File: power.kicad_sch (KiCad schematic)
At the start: 51 parts, among them U10 TPS82084SIL, U11 TPS7A8801RTJR, U12 TPS7A8801RTJR, U9 TPS82084SIL

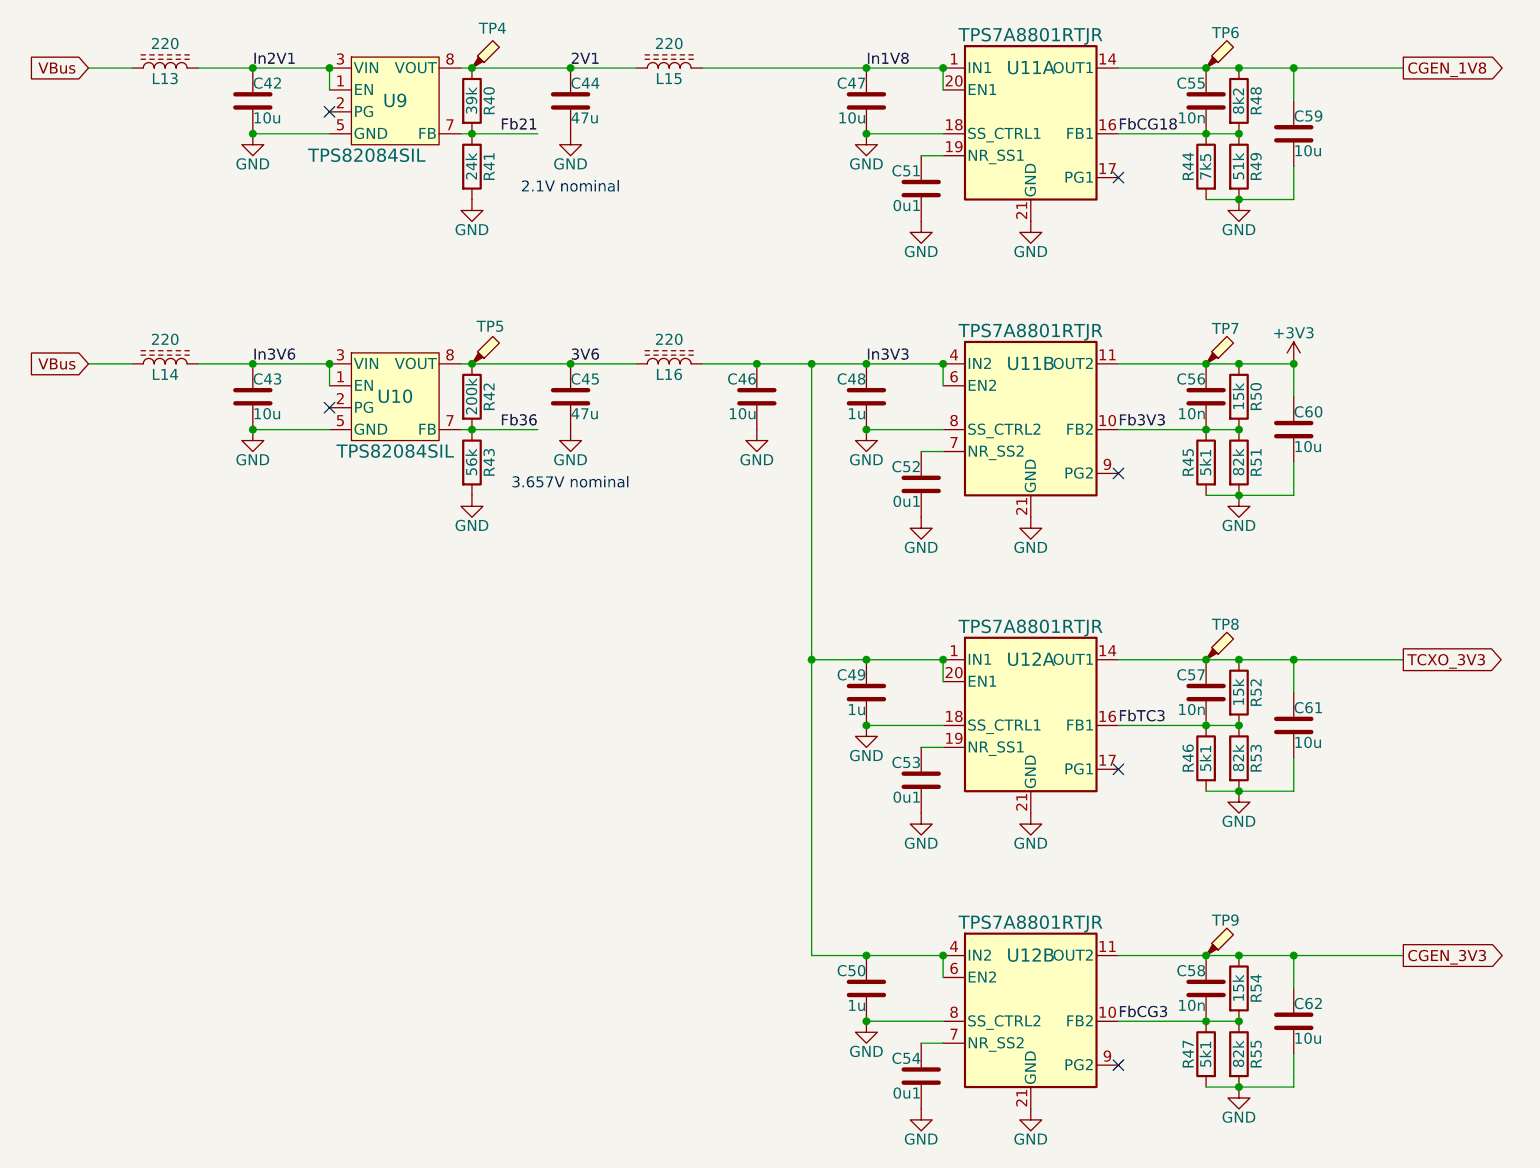
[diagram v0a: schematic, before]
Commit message: Silkscreen passes DRC.  Also we renumbered everything.
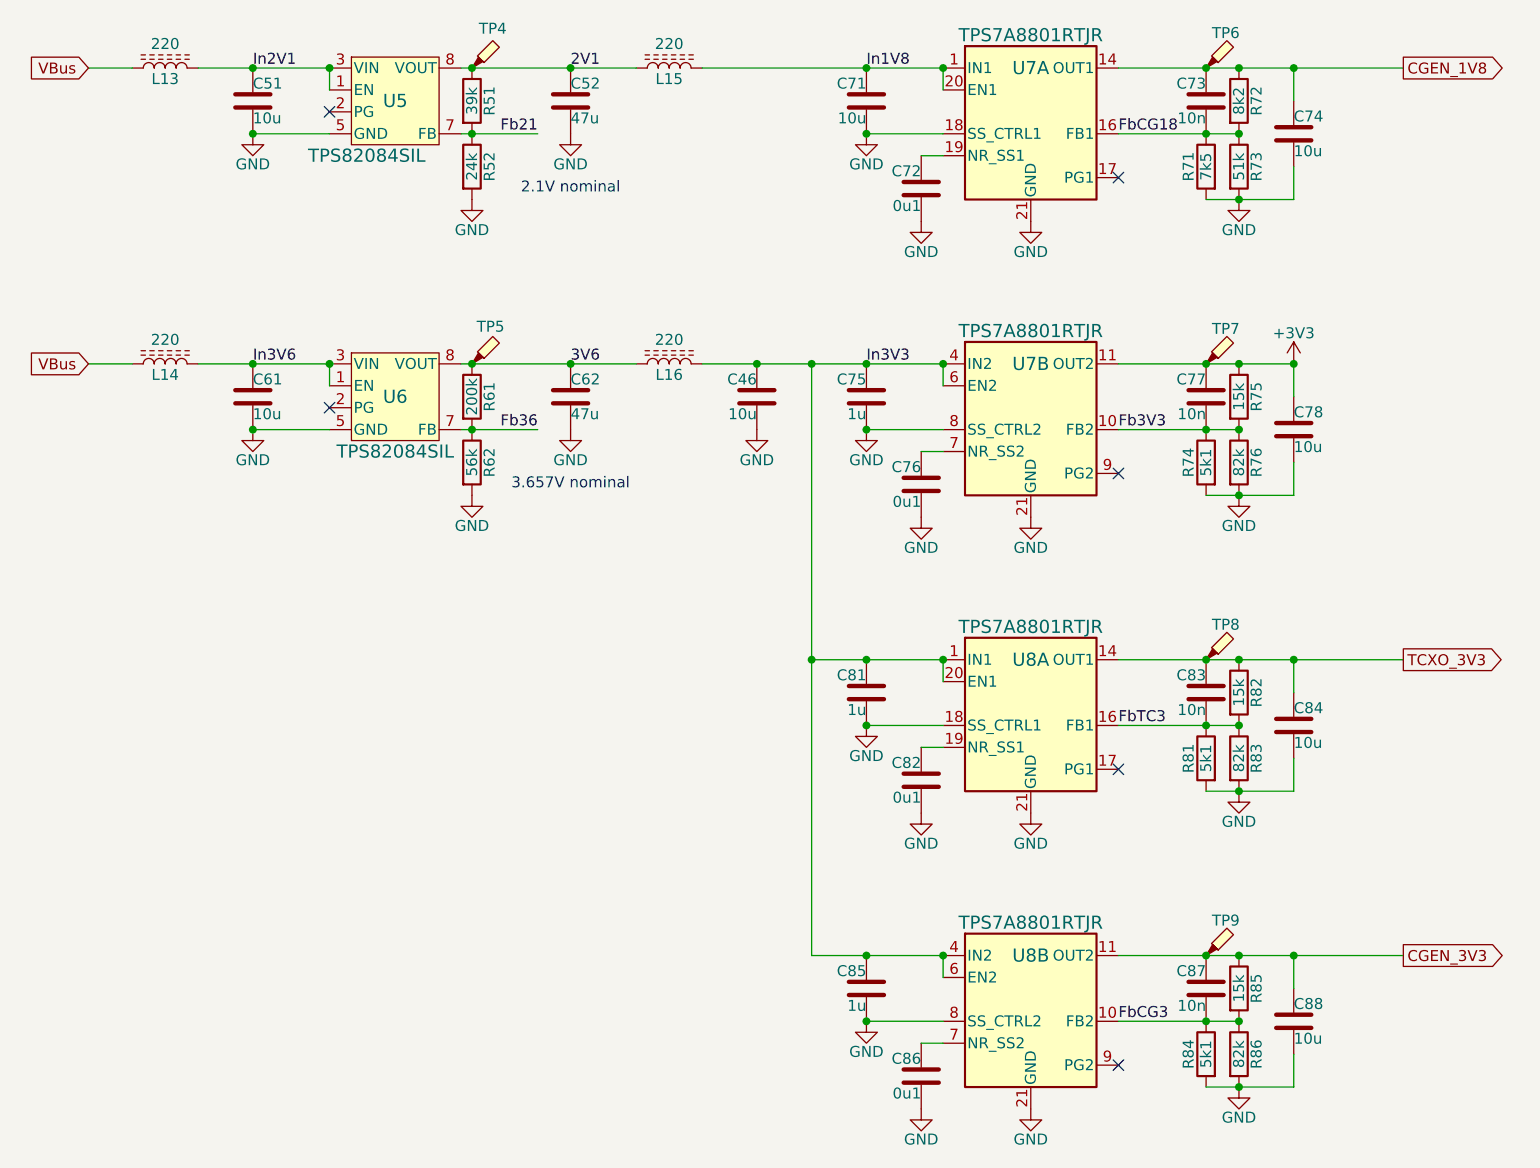
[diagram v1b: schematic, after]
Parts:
- renumbered C42 to C51, C44 to C52, C43 to C61, C45 to C62, C47 to C71, C51 to C72, C55 to C73, C59 to C74, C48 to C75, C52 to C76, C56 to C77, C60 to C78, C49 to C81, C53 to C82, C57 to C83, C61 to C84, C50 to C85, C54 to C86, C58 to C87, C62 to C88, R40 to R51, R41 to R52, R42 to R61, R43 to R62, R44 to R71, R48 to R72, R49 to R73, R45 to R74, R50 to R75, R51 to R76, R46 to R81, R52 to R82, R53 to R83, R47 to R84, R54 to R85, R55 to R86, U9 to U5, U10 to U6, U11 to U7, U12 to U8

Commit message: Sorting out part number assignments.
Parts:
- C46, C51, C61, C71, C74, C78, C84, C88: JLCPCB C15525 -> (none); LCSC (none) -> C15525
- C52, C62: JLCPCB C16780 -> (none); LCSC (none) -> C16780
- C72, C76, C82, C86: JLCPCB C307331 -> (none); LCSC (none) -> C307331
- C73, C77, C83, C87: JLCPCB C15195 -> (none); LCSC (none) -> C15195
- C75, C81, C85: JLCPCB C52923 -> (none); LCSC (none) -> C52923
- L13, L14, L15, L16: JLCPCB C14709 -> (none); LCSC (none) -> C14709
- R51: JLCPCB C25796 -> (none); LCSC (none) -> C25796
- R52: LCSC (none) -> C25769
- R61: LCSC (none) -> C25764
- R62: LCSC (none) -> C25796
- R71: JLCPCB C25918 -> (none); LCSC (none) -> C25918
- R72: JLCPCB C25924 -> (none); LCSC (none) -> C25924
- R73: JLCPCB C23196 -> (none); LCSC (none) -> C23196
- R74, R81, R84: JLCPCB C25905 -> (none); LCSC (none) -> C25905
- R75, R82, R85: JLCPCB C25756 -> (none); LCSC (none) -> C25756
- R76, R83, R86: JLCPCB C23254 -> (none); LCSC (none) -> C23254
- U5, U6: JLCPCB C468248 -> (none); LCSC (none) -> C468248
- U7, U8: JLCPCB C485919 -> (none); LCSC (none) -> C485919
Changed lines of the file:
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@@
 			)
 		)
-		(property "JLCPCB" "C25756"
-			(at 196.85 69.85 0)
+		(property "LCSC" "C25756"
+			(at 196.85 69.85 90)
 			(effects
 				(font
@@
 			)
 		)
-		(property "JLCPCB" "C307331"
+		(property "LCSC" "C307331"
 			(at 160.02 148.59 0)
 			(effects
@@
 			)
 		)
-		(property "JLCPCB" "C15525"
+		(property "LCSC" "C15525"
 			(at 203.2 39.37 0)
 			(effects
@@
 			)
 		)
-		(property "JLCPCB" "C23254"
+		(property "LCSC" "C23254"
 			(at 196.85 111.76 90)
 			(effects
@@
 			)
 		)
-		(property "JLCPCB" "C15195"
+		(property "LCSC" "C15195"
 			(at 193.04 69.85 0)
 			(effects
@@
 			)
 		)
-		(property "JLCPCB" "C23254"
+		(property "LCSC" "C23254"
 			(at 196.85 146.05 90)
 			(effects
@@
 			)
 		)
-		(property "JLCPCB" "C468248"
+		(property "LCSC" "C468248"
 			(at 99.06 35.56 0)
 			(effects
@@
 			)
 		)
-		(property "JLCPCB" "C14709"
+		(property "LCSC" "C14709"
 			(at 72.39 31.75 90)
 			(effects
@@
 			)
 		)
-		(property "JLCPCB" "C25905"
-			(at 193.04 146.05 0)
+		(property "LCSC" "C25905"
+			(at 193.04 146.05 90)
 			(effects
 				(font
@@
 			)
 		)
-		(property "JLCPCB" "C15525"
+		(property "LCSC" "C15525"
 			(at 203.2 107.95 0)
 			(effects
@@
 			)
 		)
-		(property "JLCPCB" "C14709"
+		(property "LCSC" "C14709"
 			(at 130.81 31.75 90)
 			(effects
@@
 			)
 		)
-		(property "JLCPCB" "C23196"
-			(at 196.85 43.18 0)
+		(property "LCSC" "C23196"
+			(at 196.85 43.18 90)
 			(effects
 				(font
@@
 			)
 		)
-		(property "JLCPCB" "C485919"
+		(property "LCSC" "C485919"
 			(at 172.72 38.1 0)
 			(effects
@@
 			)
 		)
-		(property "JLCPCB" "C23254"
+		(property "LCSC" "C23254"
 			(at 196.85 77.47 90)
 			(effects
@@
 			)
 		)
-		(property "JLCPCB" "C25905"
-			(at 193.04 77.47 0)
+		(property "LCSC" "C25905"
+			(at 193.04 77.47 90)
 			(effects
 				(font
@@
 			)
 		)
-		(property "JLCPCB" "C15525"
+		(property "LCSC" "C15525"
 			(at 203.2 142.24 0)
 			(effects
@@
 			)
 		)
-		(property "JLCPCB" "C25796"
-			(at 107.95 35.56 0)
+		(property "LCSC" "C25796"
+			(at 107.95 35.56 90)
 			(effects
 				(font
@@
 			)
 		)
-		(property "JLCPCB" "C15195"
+		(property "LCSC" "C15195"
 			(at 193.04 138.43 0)
 			(effects
@@
 			)
 		)
-		(property "JLCPCB" ""
-			(at 107.95 69.85 0)
+		(property "LCSC" "C25764"
+			(at 107.95 69.85 90)
 			(effects
 				(font
@@
 			)
 		)
-		(property "JLCPCB" "C52923"
+		(property "LCSC" "C52923"
 			(at 153.67 69.85 0)
 			(effects
@@
 			)
 		)
-		(property "JLCPCB" "C52923"
+		(property "LCSC" "C52923"
 			(at 153.67 104.14 0)
 			(effects
@@
 			)
 		)
-		(property "JLCPCB" "C485919"
+		(property "LCSC" "C485919"
 			(at 172.72 106.68 0)
 			(effects
@@
 			)
 		)
-		(property "JLCPCB" "C15525"
+		(property "LCSC" "C15525"
 			(at 153.67 35.56 0)
 			(effects
@@
 			)
 		)
-		(property "JLCPCB" "C25905"
-			(at 193.04 111.76 0)
+		(property "LCSC" "C25905"
+			(at 193.04 111.76 90)
 			(effects
 				(font
@@
 			)
 		)
-		(property "JLCPCB" "C16780"
+		(property "LCSC" "C16780"
 			(at 119.38 69.85 0)
 			(effects
@@
 			)
 		)
-		(property "JLCPCB" "C14709"
+		(property "LCSC" "C14709"
 			(at 72.39 66.04 90)
 			(effects
@@
 			)
 		)
-		(property "JLCPCB" "C15525"
+		(property "LCSC" "C15525"
 			(at 140.97 69.85 0)
 			(effects
@@
 			)
 		)
-		(property "JLCPCB" "C25756"
+		(property "LCSC" "C25756"
 			(at 196.85 138.43 90)
 			(effects
@@
 			)
 		)
-		(property "JLCPCB" "C485919"
+		(property "LCSC" "C485919"
 			(at 172.72 140.97 0)
 			(effects
@@
 			)
 		)
-		(property "JLCPCB" ""
-			(at 107.95 43.18 0)
+		(property "LCSC" "C25769"
+			(at 107.95 43.18 90)
 			(effects
 				(font
@@
 			)
 		)
-		(property "JLCPCB" "C25756"
+		(property "LCSC" "C25756"
 			(at 196.85 104.14 90)
 			(effects
@@
 			)
 		)
-		(property "JLCPCB" "C485919"
+		(property "LCSC" "C485919"
 			(at 172.72 72.39 0)
 			(effects
@@
 			)
 		)
-		(property "JLCPCB" "C25924"
+		(property "LCSC" "C25924"
 			(at 196.85 35.56 90)
 			(effects
@@
 			)
 		)
-		(property "JLCPCB" "C307331"
+		(property "LCSC" "C307331"
 			(at 160.02 80.01 0)
 			(effects
@@
 			)
 		)
-		(property "JLCPCB" "C16780"
+		(property "LCSC" "C16780"
 			(at 119.38 35.56 0)
 			(effects
@@
 			)
 		)
-		(property "JLCPCB" "C25918"
-			(at 193.04 43.18 0)
+		(property "LCSC" "C25918"
+			(at 193.04 43.18 90)
 			(effects
 				(font
@@
 			)
 		)
-		(property "JLCPCB" "C15195"
+		(property "LCSC" "C15195"
 			(at 193.04 104.14 0)
 			(effects
@@
 			)
 		)
-		(property "JLCPCB" "C15525"
+		(property "LCSC" "C15525"
 			(at 203.2 73.66 0)
 			(effects
@@
 			)
 		)
-		(property "JLCPCB" "C15525"
+		(property "LCSC" "C15525"
 			(at 82.55 69.85 0)
 			(effects
@@
 			)
 		)
-		(property "JLCPCB" "C15525"
+		(property "LCSC" "C15525"
 			(at 82.55 35.56 0)
 			(effects
@@
 			)
 		)
-		(property "JLCPCB" ""
-			(at 107.95 77.47 0)
+		(property "LCSC" "C25796"
+			(at 107.95 77.47 90)
 			(effects
 				(font
@@
 			)
 		)
-		(property "JLCPCB" "C15195"
+		(property "LCSC" "C15195"
 			(at 193.04 35.56 0)
 			(effects
@@
 			)
 		)
-		(property "JLCPCB" "C468248"
+		(property "LCSC" "C468248"
 			(at 99.06 69.85 0)
 			(effects
@@
 			)
 		)
-		(property "JLCPCB" "C307331"
+		(property "LCSC" "C307331"
 			(at 160.02 45.72 0)
 			(effects
@@
 			)
 		)
-		(property "JLCPCB" "C307331"
+		(property "LCSC" "C307331"
 			(at 160.02 114.3 0)
 			(effects
@@
 			)
 		)
-		(property "JLCPCB" "C14709"
+		(property "LCSC" "C14709"
 			(at 130.81 66.04 90)
 			(effects
@@
 			)
 		)
-		(property "JLCPCB" "C52923"
+		(property "LCSC" "C52923"
 			(at 153.67 138.43 0)
 			(effects

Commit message: Final fixes.  Ordered.
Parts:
- R51: LCSC C25796 -> C25783
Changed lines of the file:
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@@
 			)
 		)
-		(property "LCSC" "C25796"
+		(property "LCSC" "C25783"
 			(at 107.95 35.56 90)
+			(effects
+				(font
+					(size 1.27 1.27)
+				)
+				(hide yes)
+			)
+		)
+		(property "JLCPCB" ""
+			(at 107.95 35.56 0)
 			(effects
 				(font
@@
 			(at 119.38 35.56 0)
 			(effects
+				(font
+					(size 1.27 1.27)
+				)
+				(hide yes)
+			)
+		)
+		(property "JLCPCB" ""
+			(at 119.38 35.56 0)
+			(effects

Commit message: Schematic updates for revision mostly done.
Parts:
- C901: renamed from C81; now not fitted
- C902: renamed from C83; now not fitted
- C903: renamed from C84; now not fitted
- C904: renamed from C82; now not fitted
- C905: renamed from C85; now not fitted
- C906: renamed from C87; now not fitted
- C907: renamed from C88; now not fitted
- C908: renamed from C86; now not fitted
- R901: renamed from R82; now not fitted
- R902: renamed from R81; now not fitted
- R903: renamed from R83; now not fitted
- R904: renamed from R85; now not fitted
- R905: renamed from R84; now not fitted
- R906: renamed from R86; now not fitted
- TP901: renamed from TP8; now not fitted
- TP902: renamed from TP9; now not fitted
- U901: renamed from U8; now not fitted
- renumbered C71 to C53, C72 to C54, C73 to C55, C74 to C56, C75 to C63, C76 to C64, C77 to C65, C78 to C66, L13 to L51, L15 to L52, L14 to L53, L16 to L54, R72 to R53, R71 to R54, R73 to R55, R75 to R63, R74 to R64, R76 to R65

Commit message: Use impedance matching baluns.
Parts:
- removed C63: 1u, Capacitor_SMD:C_0402_1005Metric, symbol Device:C
- renumbered C46 to C63
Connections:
- net CGEN_1V8 renamed +1V8
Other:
- moved on the sheet: C63
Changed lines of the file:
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@@
 	)
 	(junction
+		(at 153.67 73.66)
+		(diameter 0)
+		(color 0 0 0 0)
+	)
+	(junction
 		(at 203.2 134.62)
 		(diameter 0)
@@
 	)
 	(junction
-		(at 153.67 73.66)
-		(diameter 0)
-		(color 0 0 0 0)
-	)
-	(junction
 		(at 82.55 73.66)
 		(diameter 0)
@@
 	)
 	(junction
-		(at 153.67 142.24)
-		(diameter 0)
-		(color 0 0 0 0)
-	)
-	(junction
-		(at 196.85 66.04)
+		(at 153.67 66.04)
 		(diameter 0)
 		(color 0 0 0 0)
 	)
 	(junction
-		(at 91.44 31.75)
+		(at 153.67 142.24)
 		(diameter 0)
 		(color 0 0 0 0)
 	)
 	(junction
-		(at 107.95 73.66)
+		(at 196.85 66.04)
 		(diameter 0)
 		(color 0 0 0 0)
 	)
 	(junction
-		(at 140.97 66.04)
+		(at 91.44 31.75)
 		(diameter 0)
 		(color 0 0 0 0)
 	)
 	(junction
-		(at 153.67 66.04)
+		(at 107.95 73.66)
 		(diameter 0)
 		(color 0 0 0 0)
@@
 	(wire
 		(pts
-			(xy 140.97 66.04) (xy 147.32 66.04)
-		)
-		(stroke
-			(width 0)
-			(type default)
-		)
-	)
-	(wire
-		(pts
 			(xy 203.2 134.62) (xy 215.9 134.62)
 		)
@@
 	(wire
 		(pts
-			(xy 153.67 66.04) (xy 162.56 66.04)
-		)
-		(stroke
-			(width 0)
-			(type default)
-		)
-	)
-	(wire
-		(pts
 			(xy 193.04 39.37) (xy 196.85 39.37)
 		)
@@
 	(wire
 		(pts
-			(xy 134.62 66.04) (xy 140.97 66.04)
+			(xy 134.62 66.04) (xy 147.32 66.04)
 		)
 		(stroke
@@
 	(wire
 		(pts
+			(xy 153.67 66.04) (xy 162.56 66.04)
+		)
+		(stroke
+			(width 0)
+			(type default)
+		)
+	)
+	(wire
+		(pts
 			(xy 203.2 66.04) (xy 203.2 69.85)
 		)
@@
 		)
 	)
-	(global_label "CGEN_1V8"
-		(shape output)
-		(at 215.9 31.75 0)
-		(fields_autoplaced yes)
-		(effects
-			(font
-				(size 1.27 1.27)
-			)
-			(justify left)
-		)
-		(property "Intersheetrefs" "${INTERSHEET_REFS}"
-			(at 228.3799 31.75 0)
-			(effects
-				(font
-					(size 1.27 1.27)
-				)
-				(justify left)
-			)
-		)
-	)
 	(netclass_flag ""
 		(length 2.54)
@@
 	)
 	(symbol
-		(lib_id "Device:C")
-		(at 153.67 69.85 0)
-		(mirror y)
-		(unit 1)
-		(exclude_from_sim no)
-		(in_bom yes)
-		(on_board yes)
-		(dnp no)
-		(property "Reference" "C63"
-			(at 153.67 68.58 0)
-			(effects
-				(font
-					(size 1.27 1.27)
-				)
-				(justify left bottom)
-			)
-		)
-		(property "Value" "1u"
-			(at 153.67 71.12 0)
-			(effects
-				(font
-					(size 1.27 1.27)
-				)
-				(justify left top)
-			)
-		)
-		(property "Footprint" "Capacitor_SMD:C_0402_1005Metric"
-			(at 152.7048 73.66 0)
-			(effects
-				(font
-					(size 1.27 1.27)
-				)
-				(hide yes)
-			)
-		)
-		(property "Datasheet" "~"
-			(at 153.67 69.85 0)
-			(effects
-				(font
-					(size 1.27 1.27)
-				)
-				(hide yes)
-			)
-		)
-		(property "Description" "Unpolarized capacitor"
-			(at 153.67 69.85 0)
-			(effects
-				(font
-					(size 1.27 1.27)
-				)
-				(hide yes)
-			)
-		)
-		(property "LCSC" "C52923"
-			(at 153.67 69.85 0)
-			(effects
-				(font
-					(size 1.27 1.27)
-				)
-				(hide yes)
-			)
-		)
-		(pin "1"
-		)
-		(pin "2"
-		)
-		(instances
-			(project "gpsref"
-				(path "/3160ff17-81c2-4674-af97-e8d9acaf6b65/6988b802-c4bd-48f6-b03d-8f2b1e6051d9"
-					(reference "C63")
-					(unit 1)
-				)
-			)
-		)
-	)
-	(symbol
-		(lib_id "power:GND")
-		(at 140.97 73.66 0)
+		(lib_id "power:+1V8")
+		(at 215.9 31.75 0)
 		(unit 1)
 		(exclude_from_sim no)
@@
 		(on_board yes)
 		(dnp no)
-		(property "Reference" "#PWR083"
-			(at 140.97 80.01 0)
+		(property "Reference" "#PWR059"
+			(at 215.9 35.56 0)
 			(effects
 				(font
@@
 			)
 		)
-		(property "Value" "GND"
-			(at 140.97 76.454 0)
+		(property "Value" "+1V8"
+			(at 215.9 28.194 0)
 			(effects
 				(font
 					(size 1.27 1.27)
 				)
-				(justify top)
 			)
 		)
 		(property "Footprint" ""
-			(at 140.97 73.66 0)
+			(at 215.9 31.75 0)
 			(effects
 				(font
@@
 		)
 		(property "Datasheet" ""
-			(at 140.97 73.66 0)
+			(at 215.9 31.75 0)
 			(effects
 				(font
@@
 			)
 		)
-		(property "Description" "Power symbol creates a global label with name \"GND\" , ground"
-			(at 140.97 73.66 0)
+		(property "Description" "Power symbol creates a global label with name \"+1V8\""
+			(at 215.9 31.75 0)
 			(effects
 				(font
@@
 		)
 		(instances
-			(project "gpsref"
+			(project ""
 				(path "/3160ff17-81c2-4674-af97-e8d9acaf6b65/6988b802-c4bd-48f6-b03d-8f2b1e6051d9"
-					(reference "#PWR083")
+					(reference "#PWR059")
 					(unit 1)
 				)
@@
 	(symbol
 		(lib_id "Device:C")
-		(at 140.97 69.85 0)
+		(at 153.67 69.85 0)
 		(mirror y)
 		(unit 1)
@@
 		(on_board yes)
 		(dnp no)
-		(property "Reference" "C46"
-			(at 140.97 68.58 0)
+		(property "Reference" "C63"
+			(at 153.67 68.58 0)
 			(effects
 				(font
@@
 		)
 		(property "Value" "10u"
-			(at 140.97 71.12 0)
+			(at 153.67 71.12 0)
 			(effects
 				(font
@@
 		)
 		(property "Footprint" "Capacitor_SMD:C_0402_1005Metric"
-			(at 140.0048 73.66 0)
+			(at 152.7048 73.66 0)
 			(effects
 				(font
@@
 		)
 		(property "Datasheet" "~"
-			(at 140.97 69.85 0)
+			(at 153.67 69.85 0)
 			(effects
 				(font
@@
 		)
 		(property "Description" "Unpolarized capacitor"
-			(at 140.97 69.85 0)
+			(at 153.67 69.85 0)
 			(effects
 				(font
@@
 		)
 		(property "LCSC" "C15525"
-			(at 140.97 69.85 0)
+			(at 153.67 69.85 0)
 			(effects
 				(font
@@
 			(project "gpsref"
 				(path "/3160ff17-81c2-4674-af97-e8d9acaf6b65/6988b802-c4bd-48f6-b03d-8f2b1e6051d9"
-					(reference "C46")
+					(reference "C63")
 					(unit 1)
 				)

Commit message: DRC clean-up.
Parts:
- U7, U901: footprint Package_DFN_QFN:QFN-20-1EP_4x4mm_P0.5mm_EP2.7x2.7mm -> Parts:QFN-20-1EP_4x4mm_P0.5mm_EP2.7x2.7mm
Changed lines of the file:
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@@
 			)
 		)
-		(property "Footprint" "Package_DFN_QFN:QFN-20-1EP_4x4mm_P0.5mm_EP2.7x2.7mm"
+		(property "Footprint" "Parts:QFN-20-1EP_4x4mm_P0.5mm_EP2.7x2.7mm"
 			(at 172.72 38.1 0)
 			(effects
@@
 			)
 		)
-		(property "Footprint" "Package_DFN_QFN:QFN-20-1EP_4x4mm_P0.5mm_EP2.7x2.7mm"
+		(property "Footprint" "Parts:QFN-20-1EP_4x4mm_P0.5mm_EP2.7x2.7mm"
 			(at 172.72 106.68 0)
 			(effects
@@
 			)
 		)
-		(property "Footprint" "Package_DFN_QFN:QFN-20-1EP_4x4mm_P0.5mm_EP2.7x2.7mm"
+		(property "Footprint" "Parts:QFN-20-1EP_4x4mm_P0.5mm_EP2.7x2.7mm"
 			(at 172.72 140.97 0)
 			(effects
@@
 			)
 		)
-		(property "Footprint" "Package_DFN_QFN:QFN-20-1EP_4x4mm_P0.5mm_EP2.7x2.7mm"
+		(property "Footprint" "Parts:QFN-20-1EP_4x4mm_P0.5mm_EP2.7x2.7mm"
 			(at 172.72 72.39 0)
 			(effects
